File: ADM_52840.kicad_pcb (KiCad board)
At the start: 2 copper layers, 45 x 60 mm, 44 parts, among them J1 JST, J3 Conn_01x16_Male, J4 Conn_01x19_Male, J5 JTAG, P1 USB_micro_B, Q1 DMP2045U, SW1 BTN1, SW2 BTN2, SW3 RESET, U1 HolyIOT_NRF52840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

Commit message: New Schematic
Optimisation for naming the pinout
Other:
- board text added: "P0.24"

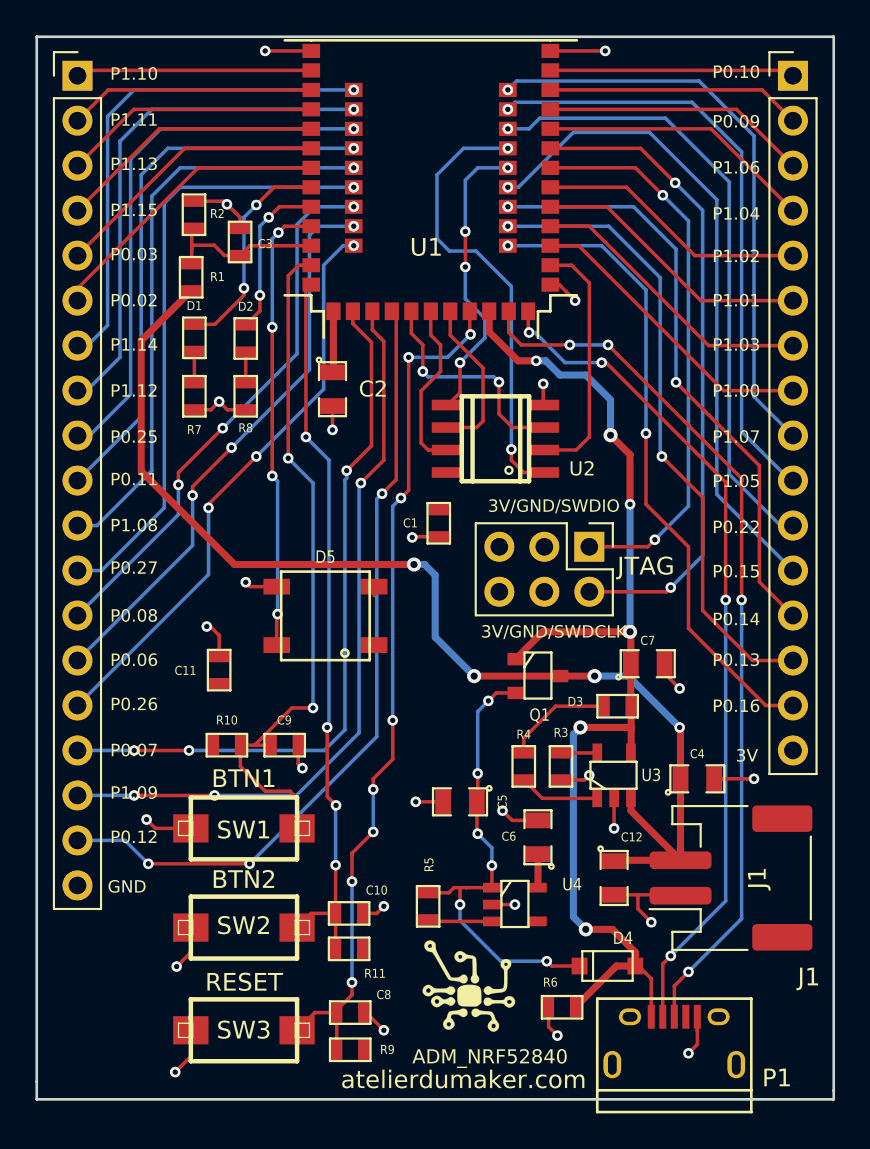
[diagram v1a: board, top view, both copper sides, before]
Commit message: Routing
Made new revision with good pinout for routing
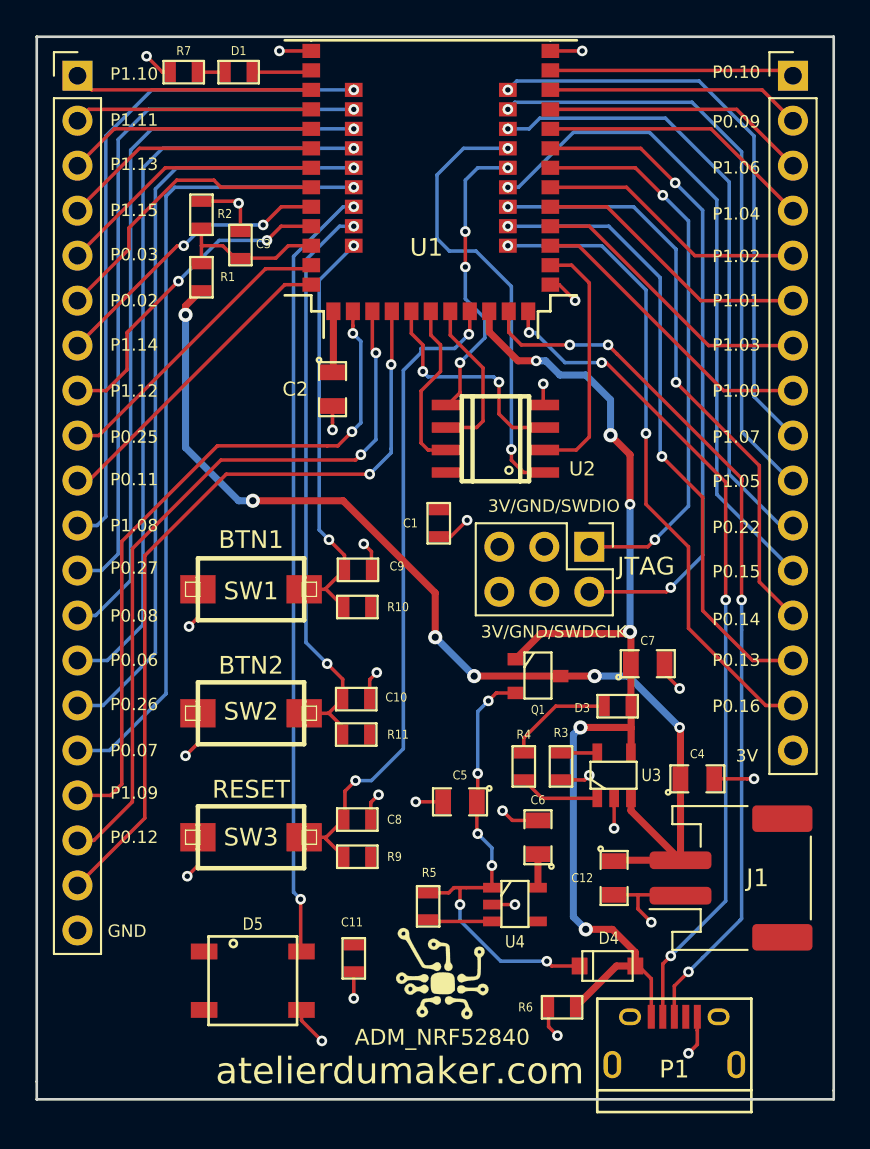
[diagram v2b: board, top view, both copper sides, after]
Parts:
- removed ?: , 
- removed D2: LED2, LEGACY:SM0603
- removed G***: LOGO, LEGACY:adm_lite
- removed G***: LOGO, LEGACY:adm
- removed R8: 330, LEGACY:SM0603
- added G1: LOGO, LEGACY:adm_lite, F.Cu at (118.9, 134.9)
- added G2: LOGO, LEGACY:adm, B.Cu at (115.9, 126.5)
- J4: value Conn_01x19_Male -> Conn_01x20_Male; footprint Connector_PinHeader_2.54mm:PinHeader_1x19_P2.54mm_Vertical -> Connector_PinHeader_2.54mm:PinHeader_1x20_P2.54mm_Vertical
- moved D5 21.0 mm to (108.2, 135.3), turned to 180 degrees
- moved R7 18.3 mm to (104.3, 84.0), turned to 180 degrees
- moved C11 18.0 mm to (113.9, 134.0), turned to 90 degrees
- moved D1 15.2 mm to (107.4, 84.0), turned to 0 degrees
- moved SW1 13.5 mm to (108.1, 113.2)
- moved SW2 12.1 mm to (108.1, 120.2)
- moved C10 12.1 mm to (114.0, 119.4)
- moved R11 12.1 mm to (114.0, 121.4)
- moved C8 10.9 mm to (114.1, 126.2)
- moved SW3 10.9 mm to (108.1, 127.2)
- moved R9 10.9 mm to (114.1, 128.3)
- moved C9 10.7 mm to (114.1, 112.1)
- moved R10 10.7 mm to (114.1, 114.2), turned to 0 degrees
- moved R1 0.58 mm to (105.3, 95.6)
- moved R2 0.42 mm to (105.3, 92.0)
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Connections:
- net P0.31 renamed BAT
- C10 pad 1: P0.05 -> BTN2
- C9 pad 1: P0.04 -> BTN1
- J4 pad 19: GND -> Net-(J4-Pad19)
- R10 pad 1: P0.04 -> BTN1
- R11 pad 1: P0.05 -> BTN2
- SW1 pad 2: P0.04 -> BTN1
- SW2 pad 2: P0.05 -> BTN2
- U1 pad 10: SK_SIGNAL -> Net-(J4-Pad8)
- U1 pad 12: P0.04 -> Net-(J4-Pad9)
- U1 pad 13: P0.05 -> Net-(J4-Pad10)
- U1 pad 14: Net-(J4-Pad7) -> Net-(J4-Pad11)
- U1 pad 15: Net-(J4-Pad8) -> Net-(J4-Pad12)
- U1 pad 16: Net-(J4-Pad9) -> Net-(J4-Pad13)
- U1 pad 17: Net-(J4-Pad10) -> Net-(J4-Pad14)
- U1 pad 18: Net-(J4-Pad11) -> Net-(J4-Pad15)
- U1 pad 19: Net-(J4-Pad12) -> Net-(J4-Pad16)
- U1 pad 2: Net-(J4-Pad1) -> Net-(D1-Pad2)
- U1 pad 20: Net-(J4-Pad13) -> SK_SIGNAL
- U1 pad 21: Net-(J4-Pad14) -> BTN2
- U1 pad 22: Net-(J4-Pad15) -> BTN1
- U1 pad 3: Net-(J4-Pad2) -> Net-(J4-Pad1)
- U1 pad 4: Net-(J4-Pad3) -> Net-(J4-Pad2)
- U1 pad 5: Net-(J4-Pad4) -> Net-(J4-Pad3)
- U1 pad 52: Net-(J4-Pad18) -> Net-(J4-Pad19)
- U1 pad 53: Net-(J4-Pad17) -> Net-(J4-Pad18)
- U1 pad 54: Net-(J4-Pad16) -> Net-(J4-Pad17)
- U1 pad 6: Net-(J4-Pad5) -> Net-(J4-Pad4)
- U1 pad 7: Net-(J4-Pad6) -> Net-(J4-Pad5)
- U1 pad 8: Net-(D1-Pad2) -> Net-(J4-Pad6)
- U1 pad 9: Net-(D2-Pad2) -> Net-(J4-Pad7)
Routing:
- net Net-(J4-Pad19): track 0.00 -> 44.5 mm, vias 0 -> 2
- net P0.05: track 40.9 -> 0.00 mm, vias 4 -> 0
- net P0.04: track 39.4 -> 0.00 mm, vias 2 -> 0
- net BTN2: track 0.00 -> 33.2 mm, vias 0 -> 2
- net BTN1: track 0.00 -> 23.9 mm, vias 0 -> 2
- net SK_SIGNAL: track 25.6 -> 44.0 mm, vias 4 -> 2
- net Net-(J4-Pad10): track 31.4 -> 17.8 mm, vias 1 -> 0
- net Net-(J4-Pad9): track 30.6 -> 17.9 mm, vias 1 -> 0
- net Net-(J4-Pad7): track 28.5 -> 16.4 mm, vias 1 -> 2
- net Net-(C8-Pad1): track 48.8 -> 37.6 mm, vias 8 -> 2
- net Net-(J4-Pad8): track 29.3 -> 18.3 mm, vias 1 -> 2
- net Net-(J4-Pad15): track 32.8 -> 43.5 mm, vias 3 -> 1
- net Net-(J4-Pad14): track 32.2 -> 42.7 mm, vias 3 -> 1
- net Net-(J4-Pad13): track 30.8 -> 41.2 mm, vias 3 -> 1
- net Net-(D2-Pad2): track 9.26 -> 0.00 mm, vias 2 -> 0
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
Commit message: PCB Routing
Trying to fit everything now that we have a goal
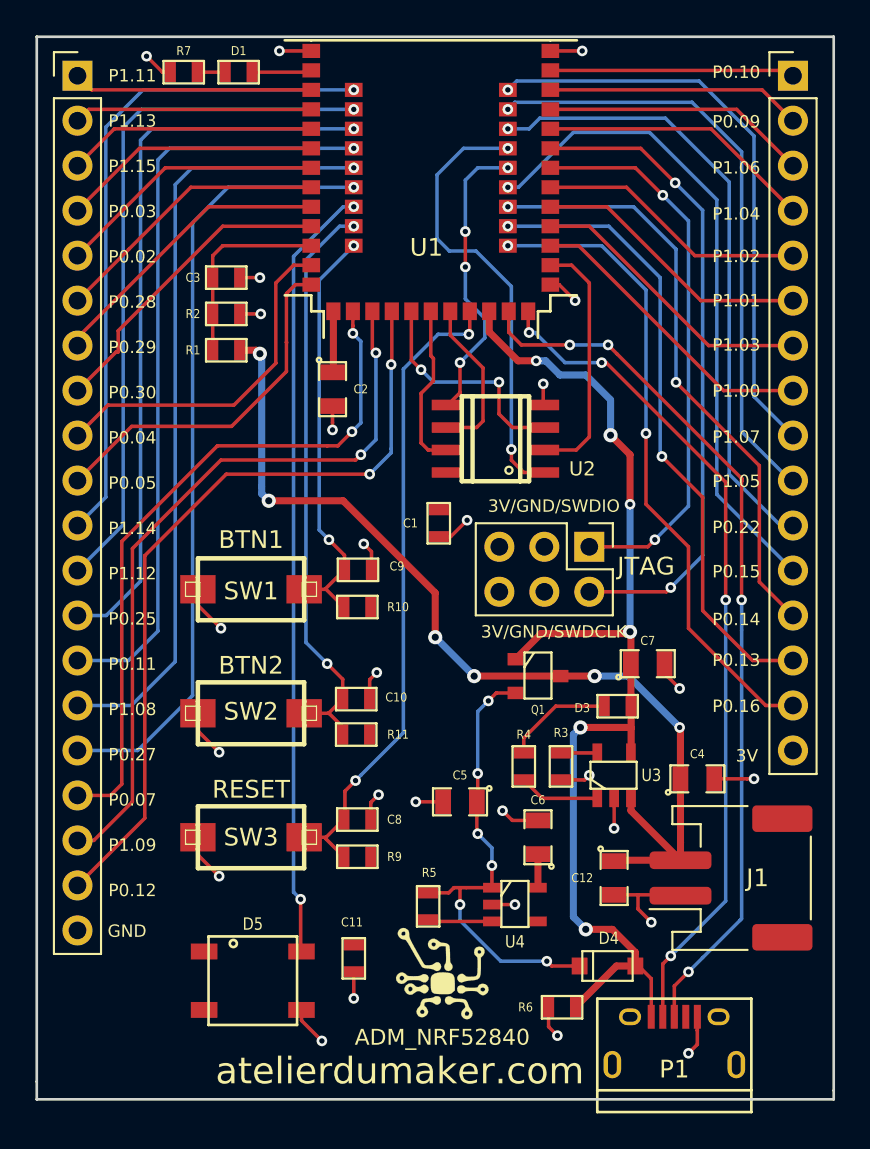
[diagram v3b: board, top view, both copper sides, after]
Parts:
- moved R2 5.77 mm to (106.7, 97.7), turned to 0 degrees
- moved R1 4.35 mm to (106.7, 99.7), turned to 180 degrees
- moved C3 2.00 mm to (106.7, 95.6), turned to 0 degrees
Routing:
- net VBAT: track 61.0 -> 55.6 mm
- net Net-(J4-Pad10): track 17.8 -> 20.4 mm
- net BAT: track 8.81 -> 11.1 mm
- net Net-(J4-Pad9): track 17.9 -> 19.8 mm
- net Net-(J4-Pad6): track 16.9 -> 15.9 mm
- net Net-(J4-Pad16): track 45.2 -> 44.4 mm
- net GND: track 53.8 -> 53.0 mm, vias 26 -> 27
- net Net-(C8-Pad1): track 37.6 -> 37.0 mm
- net Net-(J4-Pad12): track 40.1 -> 39.5 mm
- net Net-(J4-Pad8): track 18.3 -> 17.7 mm, vias 2 -> 0
- net Net-(J4-Pad7): track 16.4 -> 16.7 mm, vias 2 -> 0
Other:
- board text added: "P0.04"
- board text added: "P0.05"
- board text added: "P0.28"
- board text added: "P0.29"
- board text added: "P0.30"
- board text removed: "P0.06"
- board text removed: "P0.08"
- board text removed: "P0.26"
- board text removed: "P1.10"
